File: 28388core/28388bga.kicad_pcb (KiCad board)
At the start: 2 copper layers, 276 parts, among them IC1 F28388DZWTS, IC2 TPS62420DRCT, IC6 OPA4350EA_250, IC7 TPS3702CX33DDCT, IC8 CDCLVC1104PW, J6 2.54-2*5, J9 Conn_02x07_Odd_Even, M1 Conn_01x01_Socket, M2 Conn_01x01_Socket, M3 Conn_01x01_Socket, M4 Conn_01x01_Socket, M5 Conn_01x01_Socket, M6 Conn_01x01_Socket, M7 Conn_01x01_Socket, Q1 FMMT618TA, Q11 AT24C16C-SSHM-T, Q13 DP83822IRHBR, Q14 DP83822IRHBR, Q2 FMMT618TA, Q4 FMMT618TA, Q46 TYPEC-304-ACP16, Q7 FMMT618TA, SW1 SW_DIP_x02, SW2 SW_Push, U1 ADR423ARMZ, Y1 ECS-2520S33-250-FN-TR

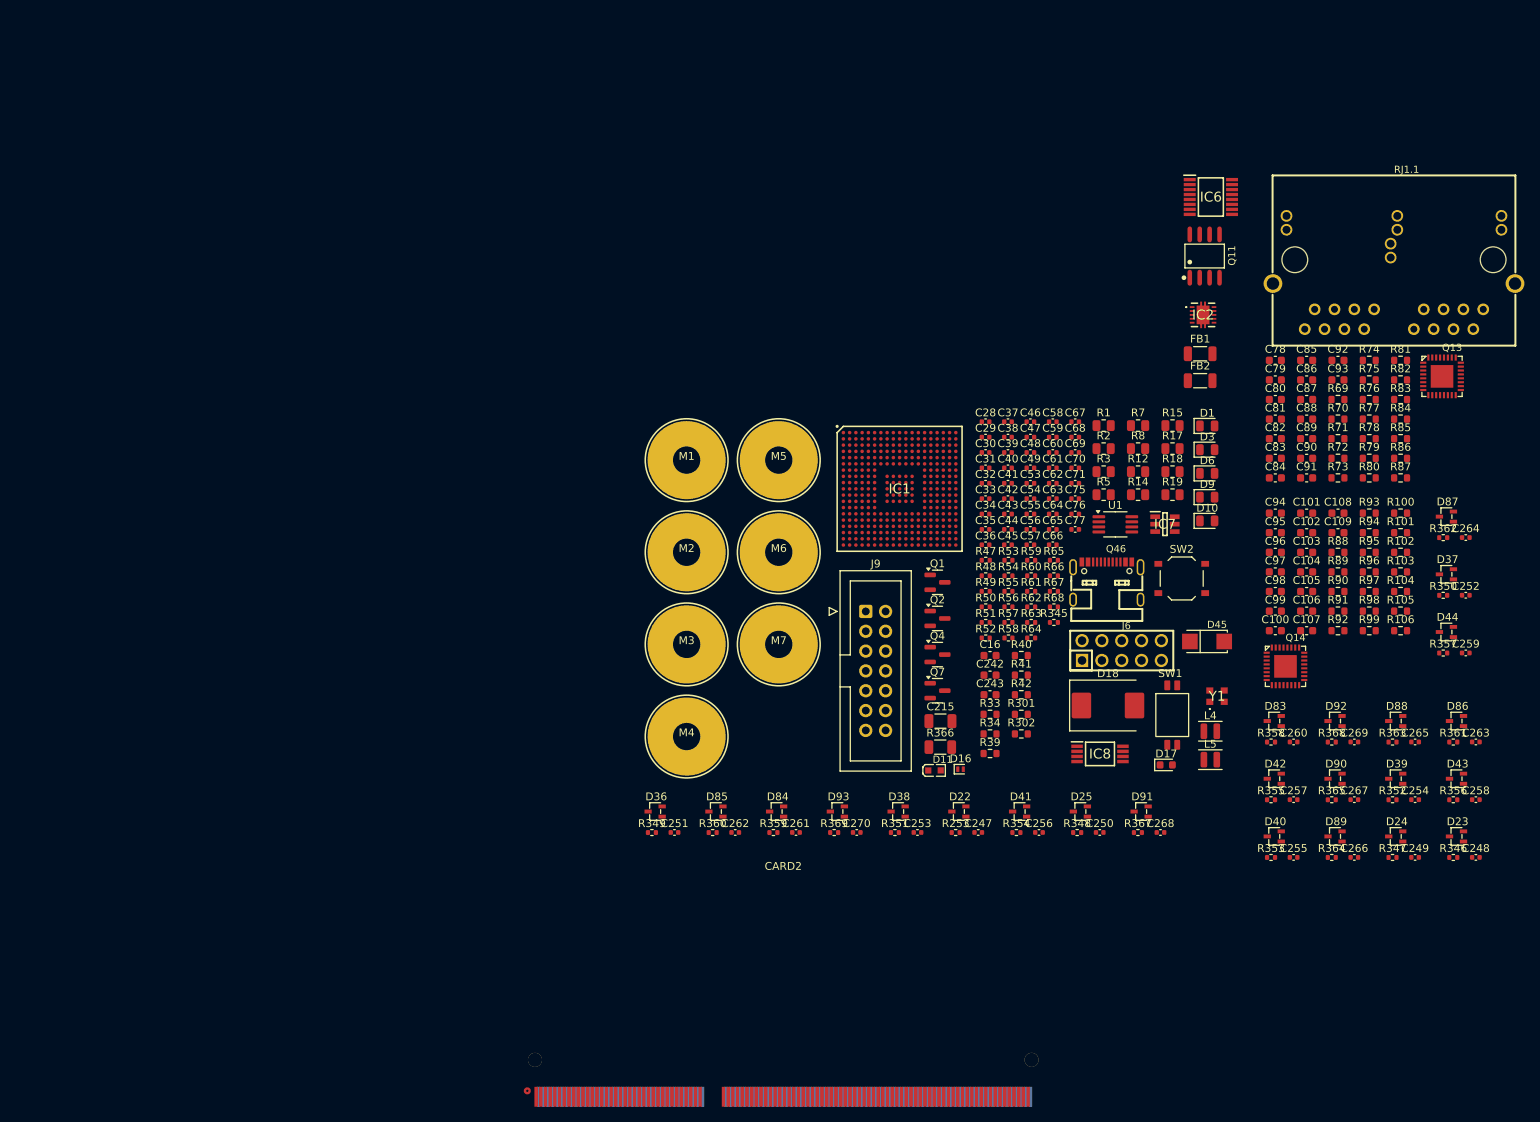
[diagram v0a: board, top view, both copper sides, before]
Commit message: 添加封装和完成引脚配对
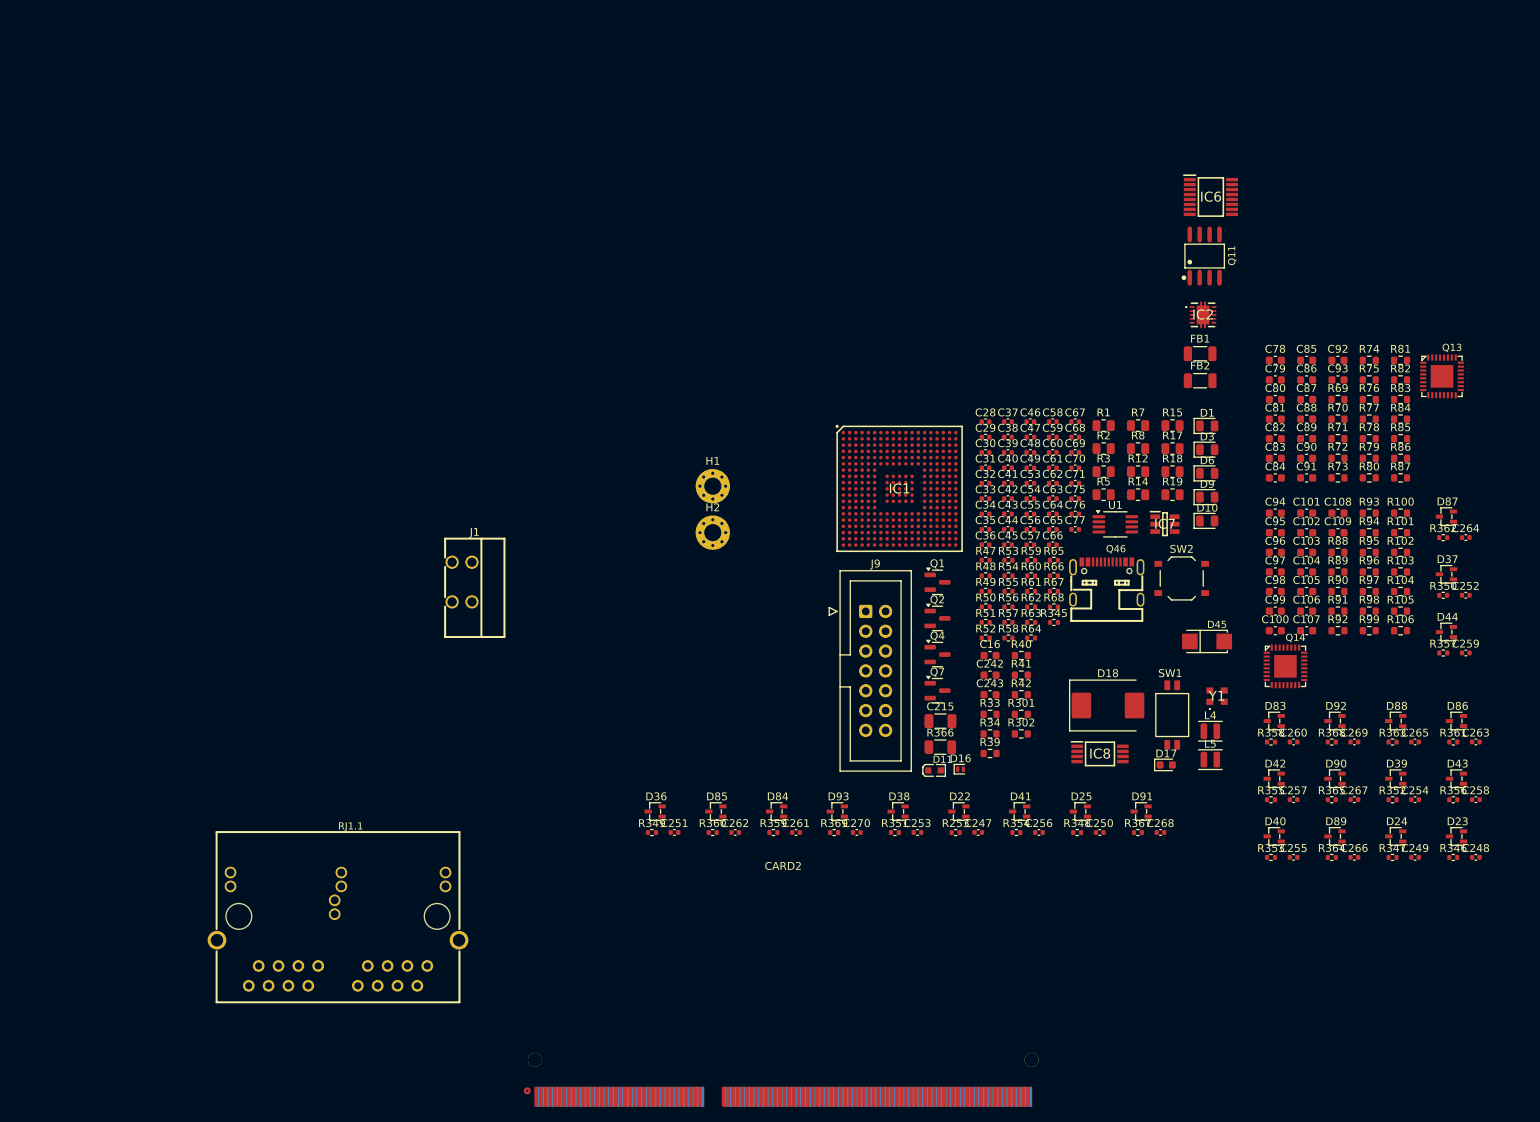
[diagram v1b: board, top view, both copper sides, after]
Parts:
- removed J6: 2.54-2*5, Lib_sheet_10:HDR-TH_10P-P2.54-V-F-R2-C5-S2.54
- removed M1, M2, M3, M4, M5, M6, M7: Conn_01x01_Socket, 1mmlab_footprint:M3
- added H1: MountingHole_Pad, MountingHole:MountingHole_2.2mm_M2_Pad_Via, F.Cu at (155.4, 79.6)
- added H2: MountingHole_Pad, MountingHole:MountingHole_2.2mm_M2_Pad_Via, F.Cu at (155.4, 85.6)
- added J1: Conn_01x02, 1mmlab_footprint:CONN-TH_2P-P2.54_DIBO_DB141R-2.54-2P, F.Cu at (123.2, 91.9)
- moved RJ1.1 159.3 mm to (107.4, 136.4)
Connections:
- net /DSP_GPIO113 renamed /GPIO113
- net /DSP_GPIO114 renamed /GPIO114
- net /DSP_GPIO118 renamed /GPIO118
- net /DSP_GPIO125 renamed /GPIO125
- net /DSP_GPIO129 renamed /ESC_TX1_EN
- net /DSP_GPIO130 renamed /ESC_TX1_CLK
- net /DSP_GPIO131 renamed /ESC_TX1_D0
- net /DSP_GPIO132 renamed /ESC_TX1_D1
- net /DSP_GPIO133 renamed /GPIO133
- net /DSP_GPIO134 renamed /ESC_TX1_D2
- net /DSP_GPIO135 renamed /ESC_TX1_D3
- net /DSP_GPIO136 renamed /ESC_RX1_DV
- net /DSP_GPIO137 renamed /ESC_RX1_CLK
- net /DSP_GPIO138 renamed /ESC_RX1_ERR
- net /DSP_GPIO139 renamed /ESC_RX1_D0
- net /DSP_GPIO140 renamed /ESC_RX1_D1
- net /DSP_GPIO141 renamed /ESC_RX1_D2
- net /DSP_GPIO142 renamed /ESC_RX1_D3
- net /DSP_GPIO143 renamed /ESC_LED_LINK0
- net /DSP_GPIO144 renamed /ESC_LED_LINK1
- net /DSP_GPIO148 renamed /ESC_PHY0
- net /DSP_GPIO149 renamed /ESC_PHY1
- net /DSP_GPIO150 renamed /ESC_I2C_SDA
- net /DSP_GPIO151 renamed /ESC_I2C_SCL
- net /DSP_GPIO152 renamed /ESC_MDC
- net /DSP_GPIO153 renamed /ESC_MDIO
- net /DSP_GPIO155 renamed /ESC_RESET
- net /DSP_GPIO156 renamed /ESC_TX0_EN
- net /DSP_GPIO157 renamed /ESC_TX0_CLK
- net /DSP_GPIO158 renamed /ESC_TX0_D0
- net /DSP_GPIO159 renamed /ESC_TX0_D1
- net /DSP_GPIO160 renamed /ESC_TX0_D2
- net /DSP_GPIO161 renamed /ESC_TX0_D3
- net /DSP_GPIO162 renamed /ESC_RX0_DV
- net /DSP_GPIO163 renamed /ESC_RX0_CLK
- net /DSP_GPIO164 renamed /ESC_RX0_ERR
- net /DSP_GPIO165 renamed /ESC_RX0_D0
- net /DSP_GPIO166 renamed /ESC_RX0_D1
- net /DSP_GPIO167 renamed /ESC_RX0_D2
- net /DSP_GPIO168 renamed /ESC_RX0_D3
- CARD2 pad 1: unconnected-(CARD2-Pad1) -> GND
- CARD2 pad 10: unconnected-(CARD2-Pad10) -> /ADC_B2_IN
- CARD2 pad 100: unconnected-(CARD2-Pad100) -> /GPIO42
- CARD2 pad 101: unconnected-(CARD2-Pad101) -> /GPIO37
- CARD2 pad 102: unconnected-(CARD2-Pad102) -> /GPIO43
- CARD2 pad 103: unconnected-(CARD2-Pad103) -> GND
- CARD2 pad 104: unconnected-(CARD2-Pad104) -> D+5V
- CARD2 pad 105: unconnected-(CARD2-Pad105) -> /GPIO44
- CARD2 pad 106: unconnected-(CARD2-Pad106) -> /GPIO50
- CARD2 pad 107: unconnected-(CARD2-Pad107) -> /GPIO45
- CARD2 pad 108: unconnected-(CARD2-Pad108) -> /GPIO51
- CARD2 pad 109: unconnected-(CARD2-Pad109) -> /GPIO46
- CARD2 pad 11: unconnected-(CARD2-Pad11) -> /ADC_A3_IN
- CARD2 pad 110: unconnected-(CARD2-Pad110) -> /GPIO52
- CARD2 pad 111: unconnected-(CARD2-Pad111) -> /GPIO47
- CARD2 pad 112: unconnected-(CARD2-Pad112) -> /GPIO53
- CARD2 pad 113: unconnected-(CARD2-Pad113) -> /GPIO48
- CARD2 pad 114: unconnected-(CARD2-Pad114) -> /GPIO54
- CARD2 pad 115: unconnected-(CARD2-Pad115) -> /GPIO49
- CARD2 pad 116: unconnected-(CARD2-Pad116) -> /GPIO55
- CARD2 pad 117: unconnected-(CARD2-Pad117) -> GND
- CARD2 pad 118: unconnected-(CARD2-Pad118) -> D+5V
- CARD2 pad 119: unconnected-(CARD2-Pad119) -> /GPIO56
- CARD2 pad 12: unconnected-(CARD2-Pad12) -> /ADC_B3_IN
- CARD2 pad 120: unconnected-(CARD2-Pad120) -> /GPIO62
- CARD2 pad 121: unconnected-(CARD2-Pad121) -> /GPIO57
- CARD2 pad 122: unconnected-(CARD2-Pad122) -> /GPIO63
- CARD2 pad 123: unconnected-(CARD2-Pad123) -> /GPIO58
- CARD2 pad 124: unconnected-(CARD2-Pad124) -> /GPIO64
- CARD2 pad 125: unconnected-(CARD2-Pad125) -> /GPIO59
- CARD2 pad 126: unconnected-(CARD2-Pad126) -> /GPIO65
- CARD2 pad 127: unconnected-(CARD2-Pad127) -> /GPIO60
- CARD2 pad 128: unconnected-(CARD2-Pad128) -> /GPIO66
- CARD2 pad 129: unconnected-(CARD2-Pad129) -> /GPIO61
- CARD2 pad 13: unconnected-(CARD2-Pad13) -> GND
- CARD2 pad 130: unconnected-(CARD2-Pad130) -> /GPIO67
- CARD2 pad 131: unconnected-(CARD2-Pad131) -> GND
- CARD2 pad 132: unconnected-(CARD2-Pad132) -> D+5V
- CARD2 pad 133: unconnected-(CARD2-Pad133) -> /GPIO68
- CARD2 pad 134: unconnected-(CARD2-Pad134) -> /GPIO74
- CARD2 pad 135: unconnected-(CARD2-Pad135) -> /GPIO69
- CARD2 pad 136: unconnected-(CARD2-Pad136) -> /GPIO75
- CARD2 pad 137: unconnected-(CARD2-Pad137) -> /GPIO70
- CARD2 pad 138: unconnected-(CARD2-Pad138) -> /GPIO76
- CARD2 pad 139: unconnected-(CARD2-Pad139) -> /GPIO71
- CARD2 pad 14: unconnected-(CARD2-Pad14) -> GND
- CARD2 pad 140: unconnected-(CARD2-Pad140) -> /GPIO77
- CARD2 pad 141: unconnected-(CARD2-Pad141) -> /GPIO72
- CARD2 pad 142: unconnected-(CARD2-Pad142) -> /GPIO78
- CARD2 pad 143: unconnected-(CARD2-Pad143) -> /GPIO73
- CARD2 pad 144: unconnected-(CARD2-Pad144) -> /GPIO79
- CARD2 pad 145: unconnected-(CARD2-Pad145) -> GND
- CARD2 pad 146: unconnected-(CARD2-Pad146) -> D+5V
- CARD2 pad 147: unconnected-(CARD2-Pad147) -> /GPIO80
- CARD2 pad 148: unconnected-(CARD2-Pad148) -> /GPIO88
- CARD2 pad 149: unconnected-(CARD2-Pad149) -> /GPIO81
- CARD2 pad 15: unconnected-(CARD2-Pad15) -> /ADC_A4_IN
- CARD2 pad 150: unconnected-(CARD2-Pad150) -> /GPIO89
- CARD2 pad 151: unconnected-(CARD2-Pad151) -> /GPIO82
- CARD2 pad 152: unconnected-(CARD2-Pad152) -> /GPIO90
- CARD2 pad 153: unconnected-(CARD2-Pad153) -> /GPIO83
- CARD2 pad 154: unconnected-(CARD2-Pad154) -> /GPIO91
- CARD2 pad 155: unconnected-(CARD2-Pad155) -> /GPIO84
- CARD2 pad 156: unconnected-(CARD2-Pad156) -> /GPIO92
- CARD2 pad 157: unconnected-(CARD2-Pad157) -> /GPIO85
- CARD2 pad 158: unconnected-(CARD2-Pad158) -> /GPIO93
- CARD2 pad 159: unconnected-(CARD2-Pad159) -> /GPIO86
- CARD2 pad 16: unconnected-(CARD2-Pad16) -> /ADC_B4_IN
- CARD2 pad 160: unconnected-(CARD2-Pad160) -> /GPIO94
- CARD2 pad 161: unconnected-(CARD2-Pad161) -> /GPIO87
- CARD2 pad 162: unconnected-(CARD2-Pad162) -> /GPIO95
- CARD2 pad 163: unconnected-(CARD2-Pad163) -> GND
- CARD2 pad 164: unconnected-(CARD2-Pad164) -> D+5V
- CARD2 pad 165: unconnected-(CARD2-Pad165) -> /GPIO96
- CARD2 pad 166: unconnected-(CARD2-Pad166) -> /GPIO102
- CARD2 pad 167: unconnected-(CARD2-Pad167) -> /GPIO97
- CARD2 pad 168: unconnected-(CARD2-Pad168) -> /GPIO103
- CARD2 pad 169: unconnected-(CARD2-Pad169) -> /GPIO98
- CARD2 pad 17: unconnected-(CARD2-Pad17) -> /ADC_A5_IN
- CARD2 pad 170: unconnected-(CARD2-Pad170) -> /GPIO104
- CARD2 pad 171: unconnected-(CARD2-Pad171) -> /GPIO99
- CARD2 pad 172: unconnected-(CARD2-Pad172) -> /GPIO105
- CARD2 pad 173: unconnected-(CARD2-Pad173) -> /GPIO100
- CARD2 pad 174: unconnected-(CARD2-Pad174) -> /GPIO106
- CARD2 pad 175: unconnected-(CARD2-Pad175) -> /GPIO101
- CARD2 pad 176: unconnected-(CARD2-Pad176) -> /GPIO107
- CARD2 pad 177: unconnected-(CARD2-Pad177) -> GND
- CARD2 pad 178: unconnected-(CARD2-Pad178) -> D+5V
- CARD2 pad 179: unconnected-(CARD2-Pad179) -> /GPIO108
- CARD2 pad 18: unconnected-(CARD2-Pad18) -> /ADC_B5_IN
- CARD2 pad 180: unconnected-(CARD2-Pad180) -> /GPIO115
- CARD2 pad 181: unconnected-(CARD2-Pad181) -> /GPIO109
- CARD2 pad 182: unconnected-(CARD2-Pad182) -> /GPIO116
- CARD2 pad 183: unconnected-(CARD2-Pad183) -> /GPIO110
- CARD2 pad 184: unconnected-(CARD2-Pad184) -> /GPIO117
- CARD2 pad 185: unconnected-(CARD2-Pad185) -> /GPIO111
- CARD2 pad 186: unconnected-(CARD2-Pad186) -> /GPIO119
- CARD2 pad 187: unconnected-(CARD2-Pad187) -> /GPIO112
- CARD2 pad 188: unconnected-(CARD2-Pad188) -> /GPIO120
- CARD2 pad 189: unconnected-(CARD2-Pad189) -> GND
- CARD2 pad 19: unconnected-(CARD2-Pad19) -> /ADC_14_IN
- CARD2 pad 190: unconnected-(CARD2-Pad190) -> D+5V
- CARD2 pad 191: unconnected-(CARD2-Pad191) -> /GPIO121
- CARD2 pad 192: unconnected-(CARD2-Pad192) -> /GPIO126
- CARD2 pad 193: unconnected-(CARD2-Pad193) -> /GPIO122
- CARD2 pad 194: unconnected-(CARD2-Pad194) -> /GPIO127
- CARD2 pad 195: unconnected-(CARD2-Pad195) -> /GPIO123
- CARD2 pad 196: unconnected-(CARD2-Pad196) -> /GPIO128
- CARD2 pad 197: unconnected-(CARD2-Pad197) -> /GPIO124
- CARD2 pad 198: unconnected-(CARD2-Pad198) -> /GPIO147
- CARD2 pad 2: unconnected-(CARD2-Pad2) -> GND
- CARD2 pad 20: unconnected-(CARD2-Pad20) -> /ADC_D0_IN
- CARD2 pad 200: unconnected-(CARD2-Pad200) -> /GPIO154
- CARD2 pad 203: unconnected-(CARD2-Pad203) -> GND
- CARD2 pad 204: unconnected-(CARD2-Pad204) -> D+5V
- CARD2 pad 21: unconnected-(CARD2-Pad21) -> /ADC_15_IN
- CARD2 pad 22: unconnected-(CARD2-Pad22) -> /ADC_D1_IN
- CARD2 pad 23: unconnected-(CARD2-Pad23) -> GND
- CARD2 pad 24: unconnected-(CARD2-Pad24) -> GND
- CARD2 pad 25: unconnected-(CARD2-Pad25) -> /ADC_C2_IN
- CARD2 pad 26: unconnected-(CARD2-Pad26) -> /ADC_D2_IN
- CARD2 pad 27: unconnected-(CARD2-Pad27) -> /ADC_C3_IN
- CARD2 pad 28: unconnected-(CARD2-Pad28) -> /ADC_D3_IN
- CARD2 pad 29: unconnected-(CARD2-Pad29) -> GND
- CARD2 pad 3: /ADC_A0 -> /ADC_A0_IN
- CARD2 pad 30: unconnected-(CARD2-Pad30) -> GND
- CARD2 pad 31: unconnected-(CARD2-Pad31) -> /ADC_C4_IN
- CARD2 pad 32: unconnected-(CARD2-Pad32) -> /ADC_D4_IN
- CARD2 pad 33: unconnected-(CARD2-Pad33) -> /ADC_C5_IN
- CARD2 pad 34: unconnected-(CARD2-Pad34) -> /ADC_D5_IN
- CARD2 pad 35: unconnected-(CARD2-Pad35) -> GND
- CARD2 pad 36: unconnected-(CARD2-Pad36) -> GND
- CARD2 pad 4: unconnected-(CARD2-Pad4) -> /ADC_B0_IN
- CARD2 pad 45: unconnected-(CARD2-Pad45) -> GND
- CARD2 pad 46: unconnected-(CARD2-Pad46) -> GND
- CARD2 pad 47: unconnected-(CARD2-Pad47) -> /GPIO0
- CARD2 pad 48: unconnected-(CARD2-Pad48) -> /GPIO4
- CARD2 pad 49: unconnected-(CARD2-Pad49) -> /GPIO1
- CARD2 pad 5: /ADC_A1 -> /ADC_A1_IN
- CARD2 pad 50: unconnected-(CARD2-Pad50) -> /GPIO5
- CARD2 pad 51: unconnected-(CARD2-Pad51) -> /GPIO2
- CARD2 pad 52: unconnected-(CARD2-Pad52) -> /GPIO6
- CARD2 pad 53: unconnected-(CARD2-Pad53) -> /GPIO3
- CARD2 pad 54: unconnected-(CARD2-Pad54) -> /GPIO7
- CARD2 pad 55: unconnected-(CARD2-Pad55) -> GND
- CARD2 pad 56: unconnected-(CARD2-Pad56) -> GND
- CARD2 pad 57: unconnected-(CARD2-Pad57) -> /GPIO8
- CARD2 pad 58: unconnected-(CARD2-Pad58) -> /GPIO12
- CARD2 pad 59: unconnected-(CARD2-Pad59) -> /GPIO9
- CARD2 pad 6: unconnected-(CARD2-Pad6) -> /ADC_B1_IN
- CARD2 pad 60: unconnected-(CARD2-Pad60) -> /GPIO13
- CARD2 pad 61: unconnected-(CARD2-Pad61) -> /GPIO10
- CARD2 pad 62: unconnected-(CARD2-Pad62) -> /GPIO14
- CARD2 pad 63: unconnected-(CARD2-Pad63) -> /GPIO11
- CARD2 pad 64: unconnected-(CARD2-Pad64) -> /GPIO15
- CARD2 pad 65: unconnected-(CARD2-Pad65) -> GND
- CARD2 pad 66: unconnected-(CARD2-Pad66) -> GND
- CARD2 pad 67: unconnected-(CARD2-Pad67) -> /GPIO16
- CARD2 pad 68: unconnected-(CARD2-Pad68) -> /GPIO18
- CARD2 pad 69: unconnected-(CARD2-Pad69) -> /GPIO17
- CARD2 pad 7: /ADC_A2 -> GND
- CARD2 pad 70: unconnected-(CARD2-Pad70) -> /GPIO19
- CARD2 pad 71: unconnected-(CARD2-Pad71) -> GND
- CARD2 pad 72: unconnected-(CARD2-Pad72) -> GND
- CARD2 pad 73: unconnected-(CARD2-Pad73) -> GND
- CARD2 pad 74: unconnected-(CARD2-Pad74) -> D+5V
- CARD2 pad 75: unconnected-(CARD2-Pad75) -> GND
- CARD2 pad 76: unconnected-(CARD2-Pad76) -> D+5V
- CARD2 pad 77: unconnected-(CARD2-Pad77) -> /GPIO20
- CARD2 pad 78: unconnected-(CARD2-Pad78) -> /GPIO26
- CARD2 pad 79: unconnected-(CARD2-Pad79) -> /GPIO21
- CARD2 pad 8: unconnected-(CARD2-Pad8) -> GND
- CARD2 pad 80: unconnected-(CARD2-Pad80) -> /GPIO27
- CARD2 pad 81: unconnected-(CARD2-Pad81) -> /GPIO22
- CARD2 pad 82: unconnected-(CARD2-Pad82) -> /GPIO28
- CARD2 pad 83: unconnected-(CARD2-Pad83) -> /GPIO23
- CARD2 pad 84: unconnected-(CARD2-Pad84) -> /GPIO29
- CARD2 pad 85: unconnected-(CARD2-Pad85) -> /GPIO24
- CARD2 pad 86: unconnected-(CARD2-Pad86) -> /GPIO30
- CARD2 pad 87: unconnected-(CARD2-Pad87) -> /GPIO25
- CARD2 pad 88: unconnected-(CARD2-Pad88) -> /GPIO31
- CARD2 pad 89: unconnected-(CARD2-Pad89) -> GND
- CARD2 pad 9: unconnected-(CARD2-Pad9) -> /ADC_A2_IN
- CARD2 pad 90: unconnected-(CARD2-Pad90) -> D+5V
- CARD2 pad 91: unconnected-(CARD2-Pad91) -> /GPIO32
- CARD2 pad 92: unconnected-(CARD2-Pad92) -> /GPIO38
- CARD2 pad 93: unconnected-(CARD2-Pad93) -> /GPIO33
- CARD2 pad 94: unconnected-(CARD2-Pad94) -> /GPIO39
- CARD2 pad 95: unconnected-(CARD2-Pad95) -> /GPIO34
- CARD2 pad 96: unconnected-(CARD2-Pad96) -> /GPIO40
- CARD2 pad 97: unconnected-(CARD2-Pad97) -> /GPIO35
- CARD2 pad 98: unconnected-(CARD2-Pad98) -> /GPIO41
- CARD2 pad 99: unconnected-(CARD2-Pad99) -> /GPIO36
- D10 pad 2: /DSP_GPIO60 -> /ESC_LED_ERR
- D11 pad 1: /DSP_GPIO61 -> /ESC_LED_RUN
- IC1 pad A11: /DSP_GPIO84 -> /GPIO84
- IC1 pad A14: /DSP_GPIO81 -> /GPIO81
- IC1 pad A15: /DSP_GPIO77 -> /GPIO77
- IC1 pad A16: /DSP_GPIO73 -> /GPIO73
- IC1 pad A17: /DSP_GPIO70 -> /GPIO70
- IC1 pad A2: /DSP_GPIO97 -> /GPIO97
- IC1 pad A3: /DSP_GPIO94 -> /GPIO94
- IC1 pad A4: /DSP_GPIO92 -> /GPIO92
- IC1 pad A5: /DSP_GPIO90 -> /GPIO90
- IC1 pad A6: /DSP_GPIO6 -> /GPIO6
- IC1 pad A7: /DSP_GPIO2 -> /GPIO2
- IC1 pad B11: /DSP_GPIO85 -> /GPIO85
- IC1 pad B12: /DSP_GPIO154 -> /GPIO154
- IC1 pad B14: /DSP_GPIO82 -> /GPIO82
- IC1 pad B15: /DSP_GPIO78 -> /GPIO78
- IC1 pad B16: /DSP_GPIO72 -> /GPIO72
- IC1 pad B17: /DSP_GPIO71 -> /GPIO71
- IC1 pad B18: /DSP_GPIO69 -> /GPIO69
- IC1 pad B19: /DSP_GPIO67 -> /GPIO67
- IC1 pad B2: /DSP_GPIO10 -> /GPIO10
- IC1 pad B3: /DSP_GPIO95 -> /GPIO95
- IC1 pad B4: /DSP_GPIO93 -> /GPIO93
- IC1 pad B5: /DSP_GPIO91 -> /GPIO91
- IC1 pad B6: /DSP_GPIO7 -> /GPIO7
- IC1 pad B7: /DSP_GPIO3 -> /GPIO3
- IC1 pad C1: /DSP_GPIO11 -> /GPIO11
- IC1 pad C11: /DSP_GPIO86 -> /GPIO86
- IC1 pad C14: /DSP_GPIO83 -> /GPIO83
- IC1 pad C15: /DSP_GPIO79 -> /GPIO79
- IC1 pad C16: /DSP_GPIO76 -> /GPIO76
- IC1 pad C17: /DSP_GPIO74 -> /GPIO74
- IC1 pad C18: /DSP_GPIO68 -> /GPIO68
- IC1 pad C19: /DSP_GPIO43 -> /GPIO43
- IC1 pad C2: /DSP_GPIO12 -> /GPIO12
- IC1 pad C3: /DSP_GPIO96 -> /GPIO96
- IC1 pad C6: /DSP_GPIO88 -> /GPIO88
- IC1 pad C7: /DSP_GPIO4 -> /GPIO4
- IC1 pad C8: /DSP_GPIO0 -> /GPIO0
- IC1 pad D1: /DSP_GPIO13 -> /GPIO13
- IC1 pad D11: /DSP_GPIO87 -> /GPIO87
- IC1 pad D15: /DSP_GPIO80 -> /GPIO80
- IC1 pad D16: /DSP_GPIO75 -> /GPIO75
- IC1 pad D17: /DSP_GPIO147 -> /GPIO147
- IC1 pad D18: /DSP_GPIO146 -> /ESC_LED_RUN
- IC1 pad D19: /DSP_GPIO42 -> /GPIO42
- IC1 pad D2: /DSP_GPIO14 -> /GPIO14
- IC1 pad D3: /DSP_GPIO15 -> /GPIO15
- IC1 pad D6: /DSP_GPIO89 -> /GPIO89
- IC1 pad D7: /DSP_GPIO5 -> /GPIO5
- IC1 pad D8: /DSP_GPIO1 -> /GPIO1
- IC1 pad E1: /DSP_GPIO16 -> /GPIO16
- IC1 pad E17: /DSP_GPIO145 -> /ESC_LED_ERR
- IC1 pad E18: /DSP_GPIO47 -> /GPIO47
- IC1 pad E19: /DSP_GPIO46 -> /GPIO46
- IC1 pad E2: /DSP_GPIO17 -> /GPIO17
- IC1 pad E3: /DSP_GPIO18 -> /GPIO18
- IC1 pad E4: /DSP_GPIO19 -> /GPIO19
- IC1 pad F1: /DSP_GPIO98 -> /GPIO98
- IC1 pad F2: /DSP_GPIO20 -> /GPIO20
- IC1 pad F3: /DSP_GPIO21 -> /GPIO21
- IC1 pad G1: /DSP_GPIO99 -> /GPIO99
- IC1 pad G2: /DSP_GPIO8 -> /GPIO8
- IC1 pad G3: /DSP_GPIO9 -> /GPIO9
- IC1 pad H1: /DSP_GPIO100 -> /GPIO100
- IC1 pad H2: /DSP_GPIO101 -> /GPIO101
- IC1 pad H3: /DSP_GPIO102 -> /GPIO102
- IC1 pad J1: /DSP_GPIO103 -> /GPIO103
- IC1 pad J16: /DSP_GPIO63 -> /GPIO63
- IC1 pad J17: /DSP_GPIO62 -> /GPIO62
- IC1 pad J2: /DSP_GPIO104 -> /GPIO104
- IC1 pad J3: /DSP_GPIO105 -> /GPIO105
- IC1 pad J4: /DSP_GPIO22 -> /GPIO22
- IC1 pad K1: /DSP_GPIO26 -> /GPIO26
- IC1 pad K16: /DSP_GPIO65 -> /GPIO65
- IC1 pad K17: /DSP_GPIO66 -> /GPIO66
- IC1 pad K18: /DSP_GPIO44 -> /GPIO44
- IC1 pad K19: /DSP_GPIO45 -> /GPIO45
- IC1 pad K2: /DSP_GPIO25 -> /GPIO25
- IC1 pad K3: /DSP_GPIO24 -> /GPIO24
- IC1 pad K4: /DSP_GPIO23 -> /GPIO23
- IC1 pad L1: /DSP_GPIO27 -> /GPIO27
- IC1 pad L16: /DSP_GPIO61 -> /GPIO61
- IC1 pad L17: /DSP_GPIO64 -> /GPIO64
- IC1 pad L2: /DSP_GPIO106 -> /GPIO106
- IC1 pad L3: /DSP_GPIO107 -> /GPIO107
- IC1 pad L4: /DSP_GPIO108 -> /GPIO108
- IC1 pad M16: /DSP_GPIO59 -> /GPIO59
- IC1 pad M17: /DSP_GPIO60 -> /GPIO60
- IC1 pad M2: /DSP_GPIO110 -> /GPIO110
- IC1 pad M3: /DSP_GPIO112 -> /GPIO112
- IC1 pad M4: /DSP_GPIO111 -> /GPIO111
- IC1 pad N16: /DSP_GPIO56 -> /GPIO56
- IC1 pad N17: /DSP_GPIO58 -> /GPIO58
- IC1 pad N18: /DSP_GPIO57 -> /GPIO57
- IC1 pad N2: /DSP_GPIO109 -> /GPIO109
- IC1 pad P16: /DSP_GPIO52 -> /GPIO52
- IC1 pad P17: /DSP_GPIO53 -> /GPIO53
- IC1 pad P18: /DSP_GPIO54 -> /GPIO54
- IC1 pad P19: /DSP_GPIO55 -> /GPIO55
- IC1 pad R16: /DSP_GPIO48 -> /GPIO48
- IC1 pad R17: /DSP_GPIO49 -> /GPIO49
- IC1 pad R18: /DSP_GPIO50 -> /GPIO50
- IC1 pad R19: /DSP_GPIO51 -> /GPIO51
- IC1 pad T11: /DSP_GPIO30 -> /GPIO30
- IC1 pad T13: /DSP_GPIO33 -> /GPIO33
- IC1 pad T14: /DSP_GPIO35 -> /GPIO35
- IC1 pad T15: /DSP_GPIO119 -> /GPIO119
- IC1 pad T16: /DSP_GPIO38 -> /GPIO38
- IC1 pad T8: /DSP_GPIO122 -> /GPIO122
- IC1 pad U11: /DSP_GPIO31 -> /GPIO31
- IC1 pad U12: /DSP_GPIO117 -> /GPIO117
- IC1 pad U13: /DSP_GPIO32 -> /GPIO32
- IC1 pad U14: /DSP_GPIO34 -> /GPIO34
- IC1 pad U15: /DSP_GPIO120 -> /GPIO120
- IC1 pad U16: /DSP_GPIO37 -> /GPIO37
- IC1 pad U17: /DSP_GPIO41 -> /GPIO41
- IC1 pad U8: /DSP_GPIO123 -> /GPIO123
- IC1 pad U9: /DSP_GPIO126 -> /GPIO126
- IC1 pad V11: /DSP_GPIO28 -> /GPIO28
- IC1 pad V12: /DSP_GPIO115 -> /GPIO115
- IC1 pad V16: /DSP_GPIO36 -> /GPIO36
- IC1 pad V17: /DSP_GPIO40 -> /GPIO40
- IC1 pad V8: /DSP_GPIO124 -> /GPIO124
- IC1 pad V9: /DSP_GPIO127 -> /GPIO127
- IC1 pad W10: /DSP_GPIO116 -> /GPIO116
- IC1 pad W11: /DSP_GPIO29 -> /GPIO29
- IC1 pad W16: /DSP_GPIO121 -> /GPIO121
- IC1 pad W17: /DSP_GPIO39 -> /GPIO39
- IC1 pad W9: /DSP_GPIO128 -> /GPIO128
- R39 pad 2: /DSP_GPIO60 -> /ESC_LED_ERR
- R40 pad 2: /DSP_GPIO61 -> /ESC_LED_RUN
- R47 pad 2: /DSP_GPIO84 -> /GPIO84
- R49 pad 2: /DSP_GPIO72 -> /GPIO72
- SW1 pad 1: /DSP_GPIO72 -> /GPIO72
- SW1 pad 2: /DSP_GPIO84 -> /GPIO84

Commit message: 添加Voltage Monitoring
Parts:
- removed D18: DNP, Diode_SMD:D_SMC
- moved RJ1.1 111.5 mm to (168.3, 42.9)
- moved H1 57.7 mm to (193.3, 36.1)
- moved H2 50.6 mm to (142.8, 36.5)
- turned IC1 to 180 degrees

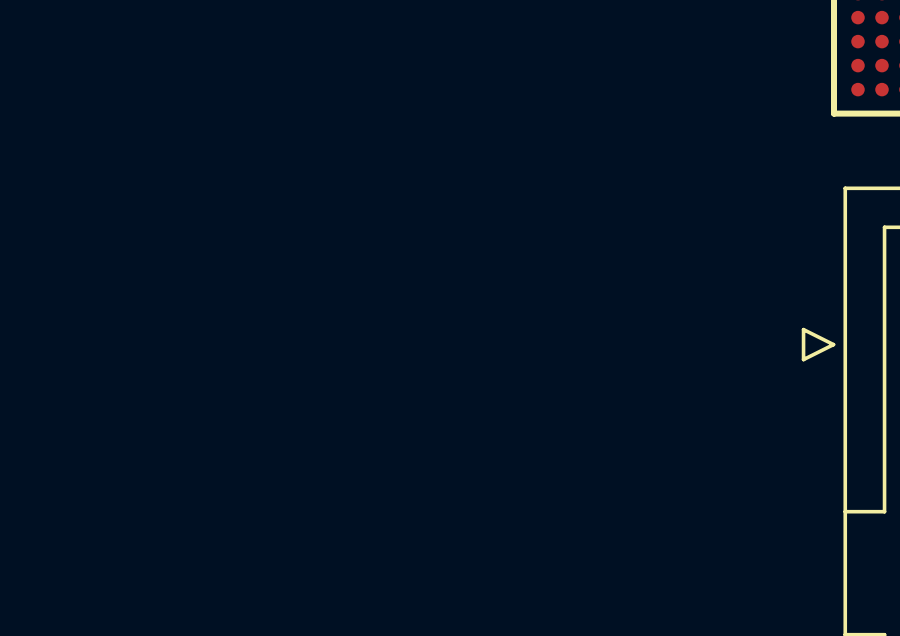
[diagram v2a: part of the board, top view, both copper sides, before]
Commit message: 只保留type-c接口供电
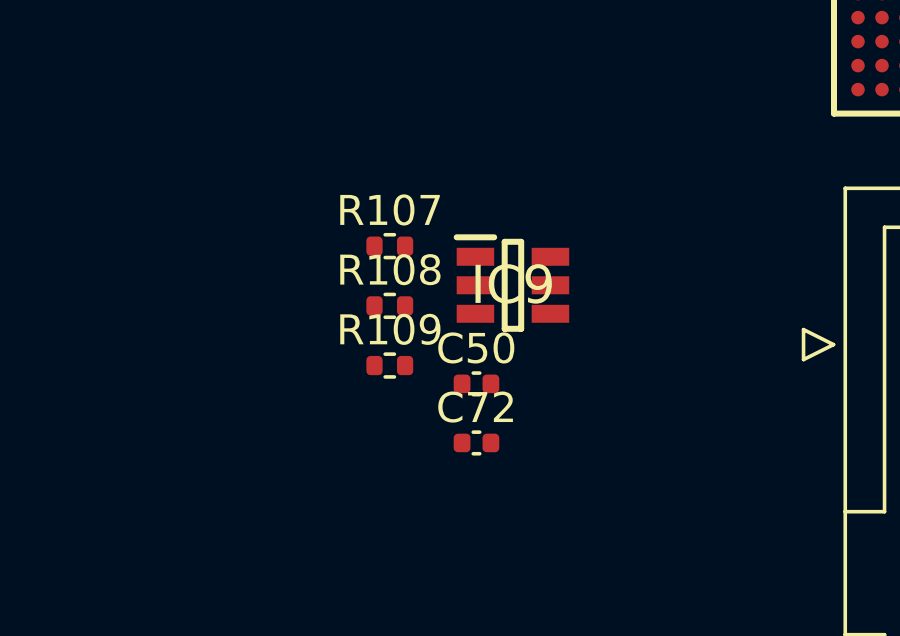
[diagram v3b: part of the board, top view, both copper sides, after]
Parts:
- added C50: 0.01uF, Capacitor_SMD:C_0402_1005Metric, F.Cu at (159.4, 97.0)
- added C72: 0.1uF, Capacitor_SMD:C_0402_1005Metric, F.Cu at (159.4, 98.9)
- added IC9: TPS3702CX12DDCT, SamacSys_Parts:SOT95P280X110-6N, F.Cu at (160.6, 93.7)
- added R107: DNP, Resistor_SMD:R_0402_1005Metric, F.Cu at (156.5, 92.4)
- added R108: DNP, Resistor_SMD:R_0402_1005Metric, F.Cu at (156.5, 94.4)
- added R109: 2.2k, Resistor_SMD:R_0402_1005Metric, F.Cu at (156.5, 96.4)
- C46: value 0.1uF -> 0.01uF
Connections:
- IC7 pad 6: unconnected-(IC7-OV-Pad6) -> Net-(IC7-OV)
- Y1 pad 1: unconnected-(Y1-TRI-STATE-Pad1) -> Net-(Y1-TRI-STATE)
